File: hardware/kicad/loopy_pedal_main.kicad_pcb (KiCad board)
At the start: 2 copper layers, 100 x 92 mm, 76 parts, among them J1 USB_C_Receptacle_USB2.0_16P, J10 Conn_01x02, J11 Conn_01x03, J2 Barrel_Jack, J3 Conn_01x06, J4 Conn_01x06, J5 Conn_01x08, J6 Conn_02x03_Odd_Even, J7 Conn_02x03_Odd_Even, J8 DIN-5_180degree, J9 DIN-5_180degree, Q1 AO3401A, SW1 SW_Push, SW2 SW_Push, U1 ATmega328P-A, U10 74AHCT1G08, U2 ATmega16U2-A, U3 AP63203WU, U4 74AHCT1G125, U5 LM66100DCK, U6 LM66100DCK, U7 USBLC6-2SC6, U8 74AHCT1G125, U9 H11L1, Y1 16MHz, Y2 16MHz

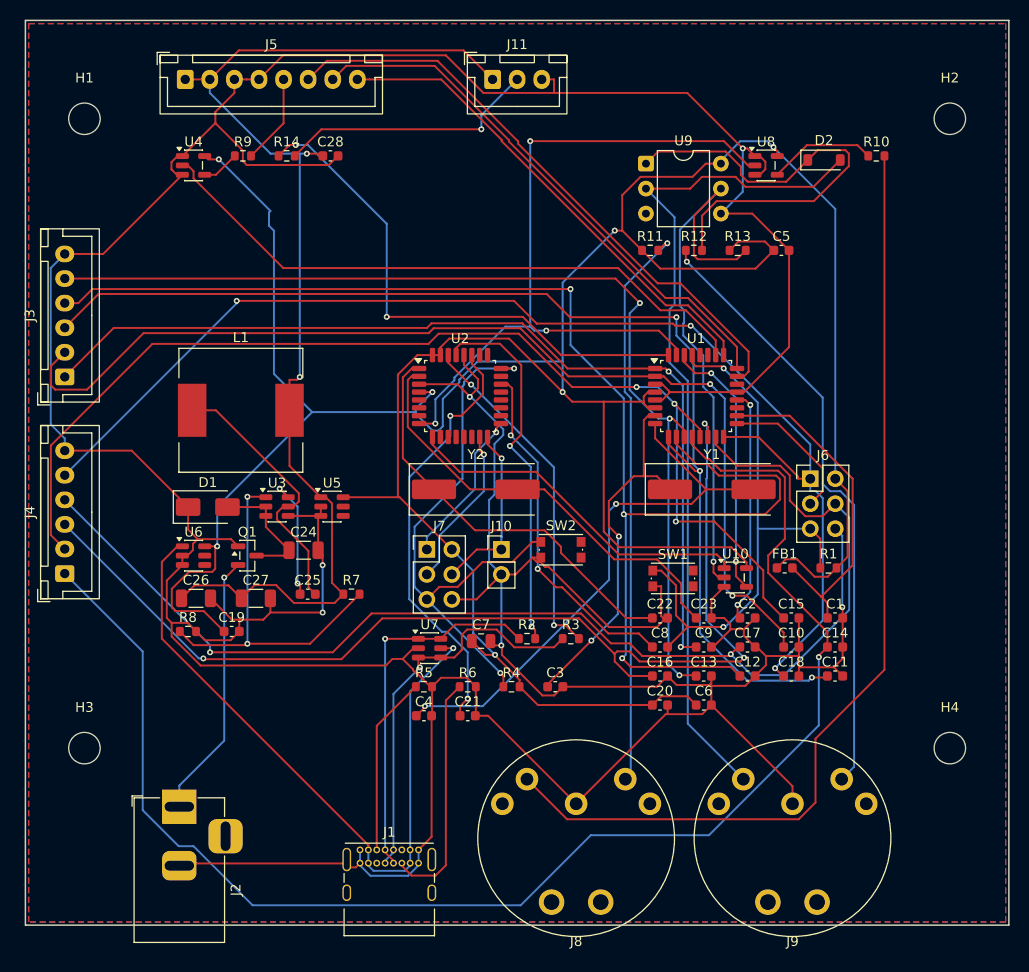
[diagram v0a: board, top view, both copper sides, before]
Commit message: fix(pcb): correct right-angle MIDI DIN footprint + body, tighter board
Reworks the MIDI jacks per feedback (didn't match a real DIN jack):
- New footprint loopy:MIDI_DIN5_RA - 5 signal pads on the standard Ø12mm DIN
  contact circle (was a splayed/incorrect pattern), with two wide-spaced
  shield/mounting posts (were only 5mm apart).
- New 3D body (box + square flange + recessed round socket via OpenSCAD)
  replacing the bare cylinder, so it reads as the real right-angle jack.
- DIN flange now sits flush at the board edge (no overhang) so the front
  signal pin clears the edge.
- Tightened the whole layout: 94x86mm (was 100x92), packing gap 1.4 -> 1.0.

(MIDI IN was already opto-isolated via U9/H11L1 + D2/1N4148 per the MIDI spec -
no change, documented explicitly now.)

Re-routed: 1053 segments / 111 vias, 0 DRC errors / 0 unrouted. Old SDS-50J
footprint removed. Gerbers + doc updated.
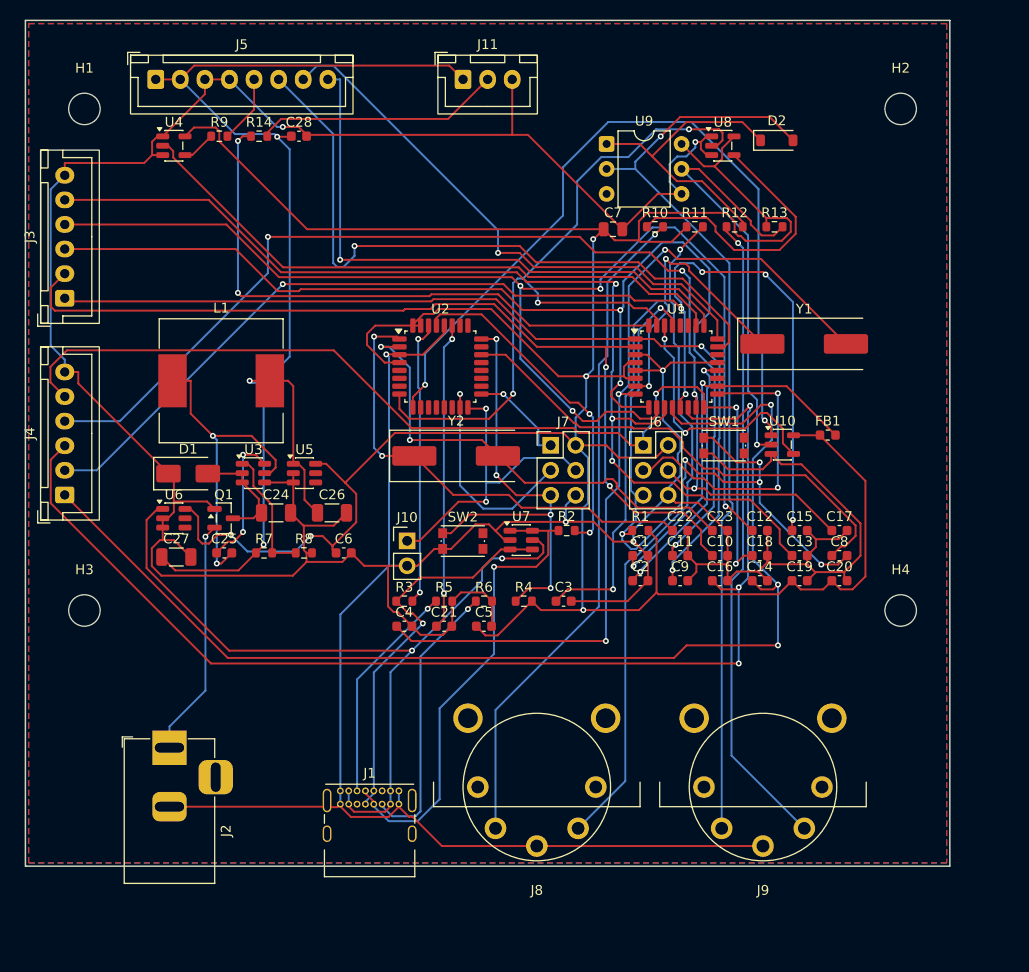
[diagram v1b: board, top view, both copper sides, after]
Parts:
- J8, J9: footprint MIDI_DIN5_SDS-50J -> MIDI_DIN5_RA
- moved C19 58.0 mm to (108.7, 87.0)
- moved C5 48.7 mm to (76.6, 91.6)
- moved C7 44.0 mm to (89.7, 51.2)
- moved C6 39.7 mm to (62.4, 84.1)
- moved R10 23.6 mm to (94.0, 51.0)
- moved C20 22.2 mm to (112.8, 87.0)
- moved C1 20.8 mm to (92.5, 84.4)
- moved C8 20.5 mm to (112.8, 84.4)
- moved C11 19.9 mm to (96.6, 84.4)
- moved R1 19.5 mm to (92.5, 81.9)
- moved Y1 17.5 mm to (109.2, 62.9)
- moved R3 17.4 mm to (68.5, 89.1)
- moved J6 17.3 mm to (92.8, 73.2)
- moved J7 16.5 mm to (83.4, 73.2)
- moved C26 16.3 mm to (61.2, 80.1)
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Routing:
- net M16_TXD: track 36.0 -> 80.9 mm, vias 0 -> 2
- net GND: track 529.8 -> 494.4 mm
- net N$17: track 100.4 -> 68.2 mm, vias 0 -> 1
- net N$4: track 56.8 -> 88.4 mm, vias 2 -> 3
- net +5V: track 347.8 -> 317.3 mm, vias 7 -> 5
- net N$3: track 37.2 -> 67.1 mm, vias 2 -> 3
- net SW_TRACK2: track 148.0 -> 121.4 mm, vias 1 -> 3
- net FB: track 37.8 -> 13.0 mm, vias 2 -> 0
- net SW_BANK: track 126.9 -> 102.5 mm
- net MIDI_OUT_BUF: track 10.9 -> 28.4 mm
- net N$5: track 14.7 -> 31.4 mm, vias 0 -> 2
- net RST_328: track 57.5 -> 74.1 mm, vias 2 -> 6
- net N$20: track 46.2 -> 30.9 mm
- net DTR: track 35.8 -> 49.9 mm, vias 2 -> 0
- net N$11: track 18.1 -> 31.7 mm, vias 1 -> 2
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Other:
- board size 100 x 92 mm -> 94 x 86 mm
